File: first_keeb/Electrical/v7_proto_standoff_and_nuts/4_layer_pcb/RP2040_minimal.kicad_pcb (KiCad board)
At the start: 4 copper layers, 77.4 x 77.1 mm, 72 parts, among them P1 USB-TYPE-C-016, Q1 SN74LV1T34DBV, SW1 SKRKAHE020, SW2 PTS647 SN70 SMTR2 LFS, SW3 PTS647 SN70 SMTR2 LFS, U1 NCP1117-3.3_SOT223, U2 LM4040DBZ-3, U3 PRTR5V0U2X, U4 W25Q32JVSS, U5 RP2040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

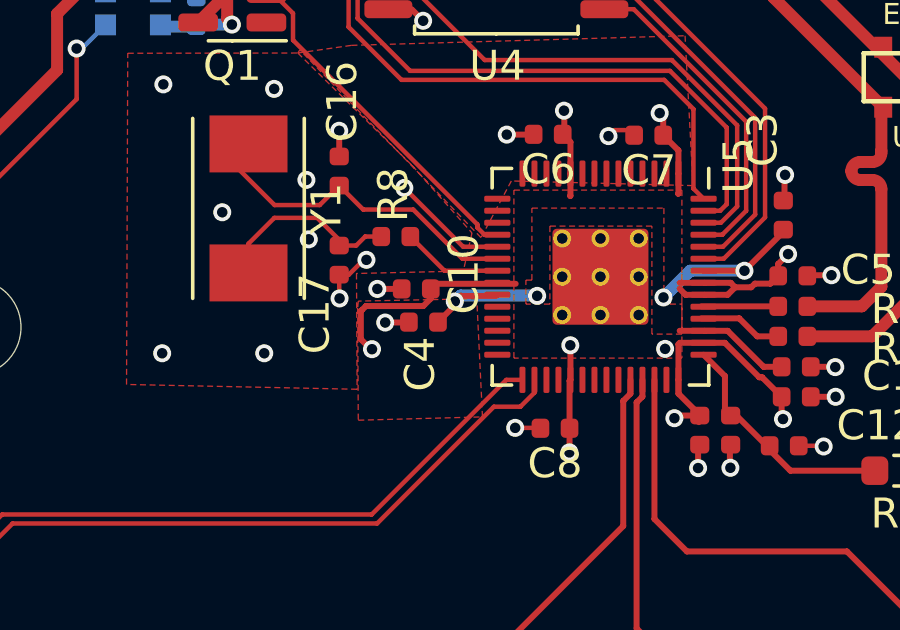
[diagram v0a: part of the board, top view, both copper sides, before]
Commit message: improve 3v3 traces in 2 layer board
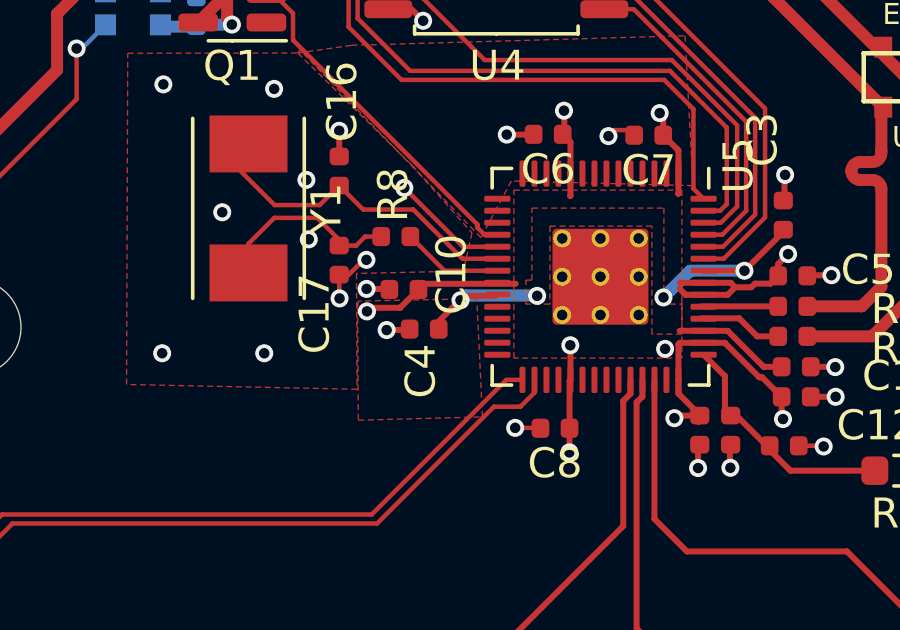
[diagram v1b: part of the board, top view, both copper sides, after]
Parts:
- moved C10 0.41 mm to (87.4, 84.7)
- moved C4 0.23 mm to (88.0, 86.1)
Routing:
- net +3V3: track 61.2 -> 59.2 mm

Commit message: improve d+/d- traces
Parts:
- moved R3 0.55 mm to (97.5, 71.1)
- moved R2 0.54 mm to (101.9, 71.1)
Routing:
- net +3V3: track 59.2 -> 57.5 mm, vias 22 -> 21
- net Net-(P1-CC2): track 2.57 -> 3.13 mm, vias 1 -> 0
- net Net-(P1-CC1): track 2.48 -> 3.02 mm, vias 1 -> 0
- net GND: track 37.2 -> 37.7 mm
- net VBUS: track 20.9 -> 21.4 mm
